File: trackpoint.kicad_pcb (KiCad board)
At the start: 2 copper layers, 27.5 x 35 mm, 32 parts, among them P1 CONN_10, P2 CONN_5, P3 CONN_8, U1 MKL03Z32VFK4, U4 ESD

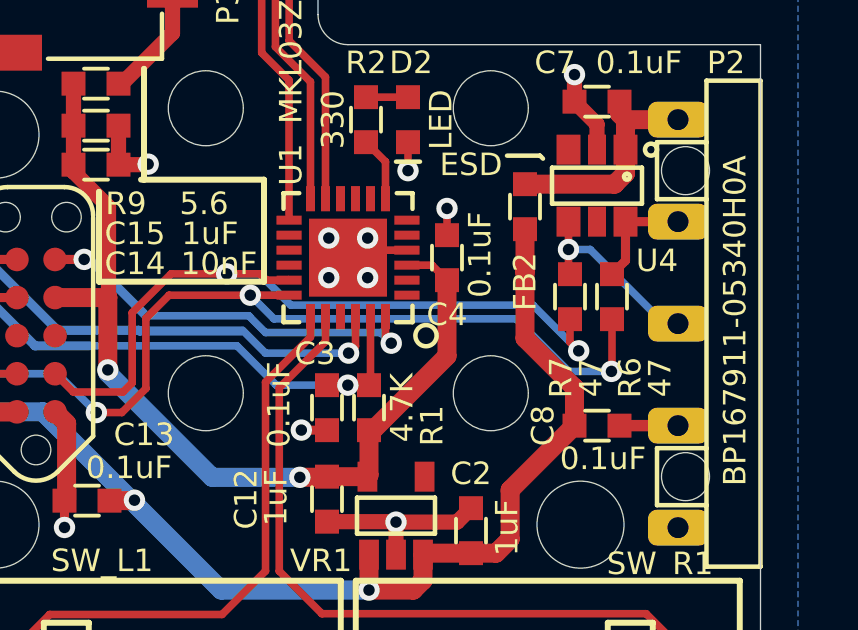
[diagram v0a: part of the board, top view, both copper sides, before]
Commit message: Adjust silk screen a tiny bit.
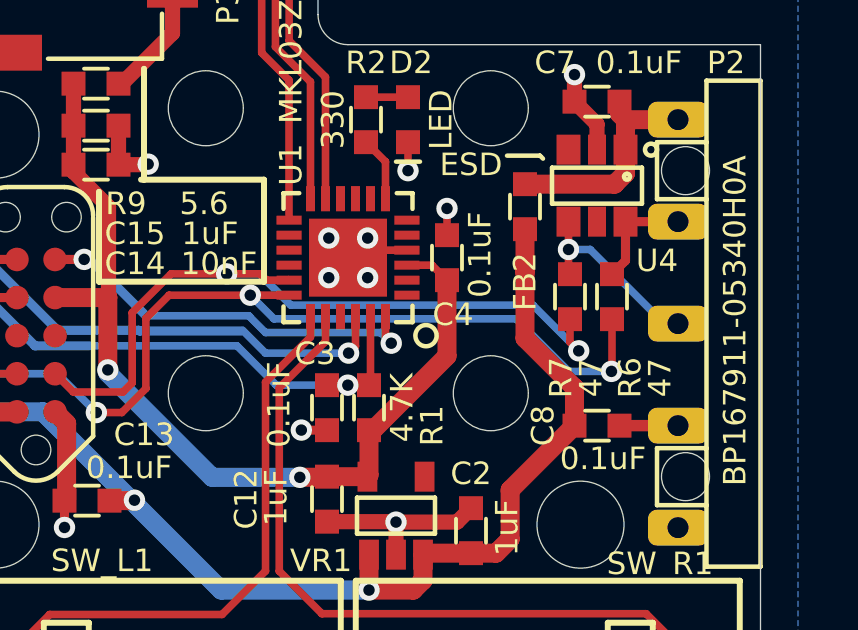
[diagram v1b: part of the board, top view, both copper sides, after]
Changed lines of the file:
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@@
     (at 209.3 130.6 270)
     (attr smd)
-    (fp_text reference C4 (at 1.9 0 180) (layer F.SilkS)
+    (fp_text reference C4 (at 1.9 -0.2 180) (layer F.SilkS)
       (effects (font (size 0.75 0.75) (thickness 0.15)))
     )

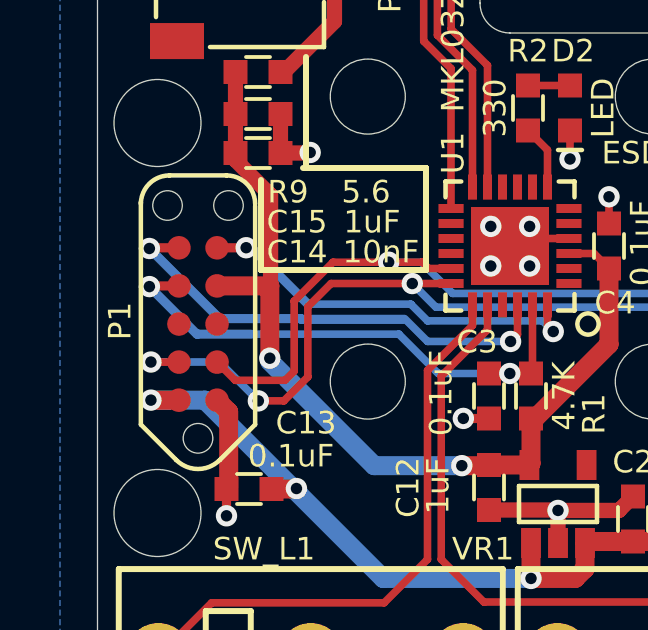
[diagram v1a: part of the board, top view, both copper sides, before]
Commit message: Add UPA14 text.
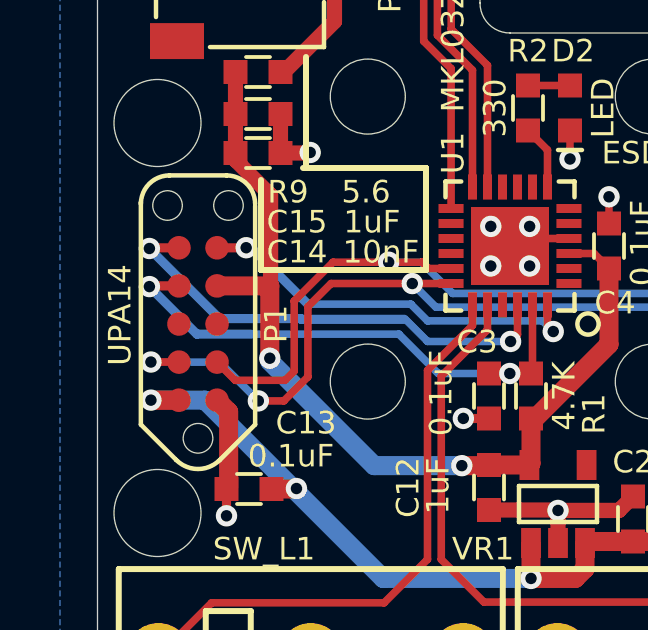
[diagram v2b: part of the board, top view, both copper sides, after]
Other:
- board text added: "UPA14"
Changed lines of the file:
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@@
   (general
     (thickness 1.6)
-    (drawings 28)
+    (drawings 29)
     (tracks 221)
     (zones 0)
@@
     (tags "Tag-Connect TC2050")
     (attr virtual)
-    (fp_text reference P1 (at 0.1 -2.6 90) (layer F.SilkS)
+    (fp_text reference P1 (at 0 2.6 90) (layer F.SilkS)
       (effects (font (size 0.75 0.75) (thickness 0.15)))
     )
@@
       (clearance 0.00001))
   )
+  (gr_text UPA14 (at 193 132.9 90) (layer F.SilkS)
+    (effects (font (size 0.75 0.75) (thickness 0.15)))
+  )
   (gr_text BP167911-05340H0A (at 218.9 132.7 90) (layer F.SilkS)

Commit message: Rename UPA14 to UPA10.
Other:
- board text added: "UPA10"
- board text removed: "UPA14"
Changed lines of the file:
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@@
-(kicad_pcb (version 20171130) (host pcbnew 5.1.3-ffb9f22~84~ubuntu18.04.1)
+(kicad_pcb (version 20171130) (host pcbnew 5.1.4-e60b266~84~ubuntu18.04.1)
   (general
     (thickness 1.6)
@@
       (clearance 0.00001))
   )
-  (gr_text UPA14 (at 193 132.9 90) (layer F.SilkS)
+  (gr_text UPA10 (at 193 132.9 90) (layer F.SilkS)
     (effects (font (size 0.75 0.75) (thickness 0.15)))
   )

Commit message: Update hole footprints and apply correct clearances.
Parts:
- removed the ? at (194.2, 126.5)
- removed the ? at (213.8, 139.5)
- removed the ? at (194.2, 139.5)
- removed the ? at (210.8, 135.1)
- removed the ? at (201.3, 135.1)
- removed the ? at (201.3, 125.6)
- removed the ? at (210.8, 125.6)
- added ?: , ugl:hole_2.9mm, F.Cu at (194.2, 126.5)
- added ?: , ugl:hole_2.9mm, F.Cu at (213.8, 139.5)
- added ?: , ugl:hole_2.9mm, F.Cu at (194.2, 139.5)
- added ?: , ugl:hole_2.5mm, F.Cu at (210.8, 135.1)
- added ?: , ugl:hole_2.5mm, F.Cu at (210.8, 125.6)
- added ?: , ugl:hole_2.5mm, F.Cu at (201.3, 135.1)
- added ?: , ugl:hole_2.5mm, F.Cu at (201.3, 125.6)

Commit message: Update microswitches.
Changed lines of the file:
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@@
     (add_net "Net-(VR1-Pad4)")
+  )
+  (module ugl:CMI126603D08 locked (layer F.Cu)
+    (at 212.660004 144.268997 180)
+    (fp_text reference SW_R1 (at -3.739996 3.468997) (layer F.SilkS)
+      (effects (font (size 0.75 0.75) (thickness 0.15)))
+    )
+    (fp_text value CMI126603D08 (at 2.060004 -2.231003) (layer F.SilkS)
+      (effects (font (size 0.75 0.75) (thickness 0.15)))
+    )
+    (fp_line (start -3.5 1.5) (end -3.5 -1.5) (layer F.SilkS) (width 0.2))
+    (fp_line (start -2 1.5) (end -3.5 1.5) (layer F.SilkS) (width 0.2))
+    (fp_line (start -2 -1.5) (end -2 1.5) (layer F.SilkS) (width 0.2))
+    (fp_line (start -3.5 -1.5) (end -2 -1.5) (layer F.SilkS) (width 0.2))
+    (fp_line (start 6.4 -2.9) (end 6.4 2.9) (layer F.SilkS) (width 0.2))
+    (fp_line (start -6.4 2.9) (end 6.4 2.9) (layer F.SilkS) (width 0.2))
+    (fp_line (start -6.4 -2.9) (end -6.4 2.9) (layer F.SilkS) (width 0.2))
+    (fp_line (start 6.4 -2.9) (end -6.4 -2.9) (layer F.SilkS) (width 0.2))
+    (pad "" np_thru_hole circle (at 5.08 0 180) (size 1.2 1.2) (drill 1.2) (layers *.Cu *.Mask))
+    (pad 2 thru_hole circle (at 0 0 180) (size 2.2 2.2) (drill 1.2) (layers *.Cu *.Mask)
+      (net 4 GND))
+    (pad 1 thru_hole circle (at -5.08 0 180) (size 2.2 2.2) (drill 1.2) (layers *.Cu *.Mask)
+      (net 27 /KEY_MRIGHT))
+  )
+  (module ugl:CMI126603D08 locked (layer F.Cu)
+    (at 199.360001 144.268997)
+    (fp_text reference SW_L1 (at -1.560001 -3.568997) (layer F.SilkS)
+      (effects (font (size 0.75 0.75) (thickness 0.15)))
+    )
+    (fp_text value CMI126603D08 (at 2.039999 2.231003) (layer F.SilkS)
+      (effects (font (size 0.75 0.75) (thickness 0.15)))
+    )
+    (fp_line (start -3.5 1.5) (end -3.5 -1.5) (layer F.SilkS) (width 0.2))
+    (fp_line (start -2 1.5) (end -3.5 1.5) (layer F.SilkS) (width 0.2))
+    (fp_line (start -2 -1.5) (end -2 1.5) (layer F.SilkS) (width 0.2))
+    (fp_line (start -3.5 -1.5) (end -2 -1.5) (layer F.SilkS) (width 0.2))
+    (fp_line (start 6.4 -2.9) (end 6.4 2.9) (layer F.SilkS) (width 0.2))
+    (fp_line (start -6.4 2.9) (end 6.4 2.9) (layer F.SilkS) (width 0.2))
+    (fp_line (start -6.4 -2.9) (end -6.4 2.9) (layer F.SilkS) (width 0.2))
+    (fp_line (start 6.4 -2.9) (end -6.4 -2.9) (layer F.SilkS) (width 0.2))
+    (pad "" np_thru_hole circle (at 5.08 0) (size 1.2 1.2) (drill 1.2) (layers *.Cu *.Mask))
+    (pad 2 thru_hole circle (at 0 0) (size 2.2 2.2) (drill 1.2) (layers *.Cu *.Mask)
+      (net 4 GND))
+    (pad 1 thru_hole circle (at -5.08 0) (size 2.2 2.2) (drill 1.2) (layers *.Cu *.Mask)
+      (net 29 /KEY_MLEFT))
   )
   (module ugl:hole_2.9mm locked (layer F.Cu)
@@
       (xy 2.621935 -1.146433)) (layer B.Mask) (width 0.01))
   )
-  (module ugl:CMI126603D08 locked (layer F.Cu)
-    (at 199.360001 144.268997)
-    (fp_text reference SW_L1 (at -1.560001 -3.568997) (layer F.SilkS)
-      (effects (font (size 0.75 0.75) (thickness 0.15)))
-    )
-    (fp_text value CMI126603D08 (at 2.039999 2.231003) (layer F.SilkS)
-      (effects (font (size 0.75 0.75) (thickness 0.15)))
-    )
-    (fp_line (start -3.5 1.5) (end -3.5 -1.5) (layer F.SilkS) (width 0.2))
-    (fp_line (start -2 1.5) (end -3.5 1.5) (layer F.SilkS) (width 0.2))
-    (fp_line (start -2 -1.5) (end -2 1.5) (layer F.SilkS) (width 0.2))
-    (fp_line (start -3.5 -1.5) (end -2 -1.5) (layer F.SilkS) (width 0.2))
-    (fp_line (start 6.4 -2.9) (end 6.4 2.9) (layer F.SilkS) (width 0.2))
-    (fp_line (start -6.4 2.9) (end 6.4 2.9) (layer F.SilkS) (width 0.2))
-    (fp_line (start -6.4 -2.9) (end -6.4 2.9) (layer F.SilkS) (width 0.2))
-    (fp_line (start 6.4 -2.9) (end -6.4 -2.9) (layer F.SilkS) (width 0.2))
-    (pad 3 thru_hole circle (at 5.08 0) (size 2.2 2.2) (drill 1.2) (layers *.Cu *.Mask))
-    (pad 2 thru_hole circle (at 0 0) (size 2.2 2.2) (drill 1.2) (layers *.Cu *.Mask)
-      (net 4 GND))
-    (pad 1 thru_hole circle (at -5.08 0) (size 2.2 2.2) (drill 1.2) (layers *.Cu *.Mask)
-      (net 29 /KEY_MLEFT))
-  )
-  (module ugl:CMI126603D08 locked (layer F.Cu)
-    (at 212.660004 144.268997 180)
-    (fp_text reference SW_R1 (at -3.739996 3.468997) (layer F.SilkS)
-      (effects (font (size 0.75 0.75) (thickness 0.15)))
-    )
-    (fp_text value CMI126603D08 (at 2.060004 -2.231003) (layer F.SilkS)
-      (effects (font (size 0.75 0.75) (thickness 0.15)))
-    )
-    (fp_line (start -3.5 1.5) (end -3.5 -1.5) (layer F.SilkS) (width 0.2))
-    (fp_line (start -2 1.5) (end -3.5 1.5) (layer F.SilkS) (width 0.2))
-    (fp_line (start -2 -1.5) (end -2 1.5) (layer F.SilkS) (width 0.2))
-    (fp_line (start -3.5 -1.5) (end -2 -1.5) (layer F.SilkS) (width 0.2))
-    (fp_line (start 6.4 -2.9) (end 6.4 2.9) (layer F.SilkS) (width 0.2))
-    (fp_line (start -6.4 2.9) (end 6.4 2.9) (layer F.SilkS) (width 0.2))
-    (fp_line (start -6.4 -2.9) (end -6.4 2.9) (layer F.SilkS) (width 0.2))
-    (fp_line (start 6.4 -2.9) (end -6.4 -2.9) (layer F.SilkS) (width 0.2))
-    (pad 3 thru_hole circle (at 5.08 0 180) (size 2.2 2.2) (drill 1.2) (layers *.Cu *.Mask))
-    (pad 2 thru_hole circle (at 0 0 180) (size 2.2 2.2) (drill 1.2) (layers *.Cu *.Mask)
-      (net 4 GND))
-    (pad 1 thru_hole circle (at -5.08 0 180) (size 2.2 2.2) (drill 1.2) (layers *.Cu *.Mask)
-      (net 27 /KEY_MRIGHT))
-  )
   (module ugl:QFN-24-1EP_4x4mm_Pitch0.5mm (layer F.Cu)

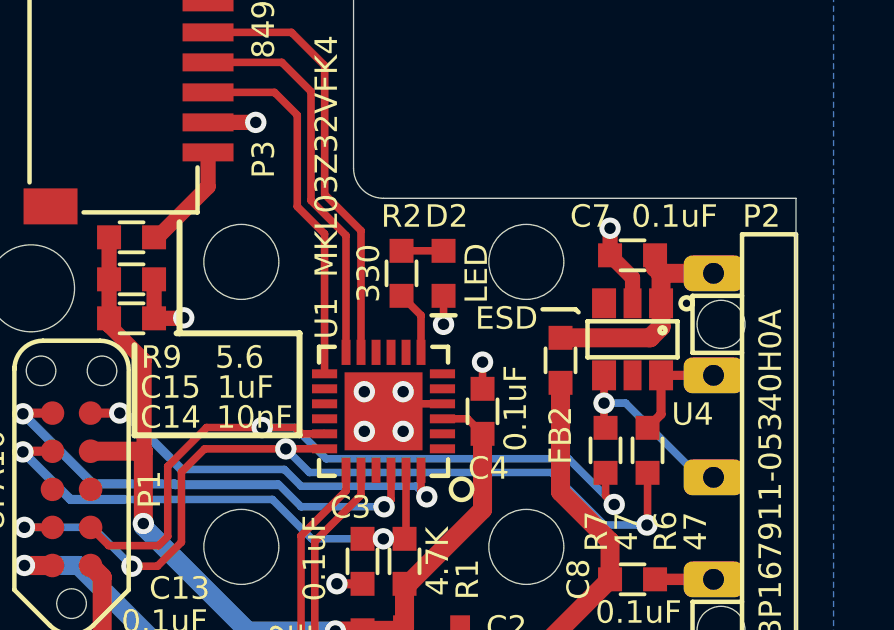
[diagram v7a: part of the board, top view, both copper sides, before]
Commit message: Update LED footprint.
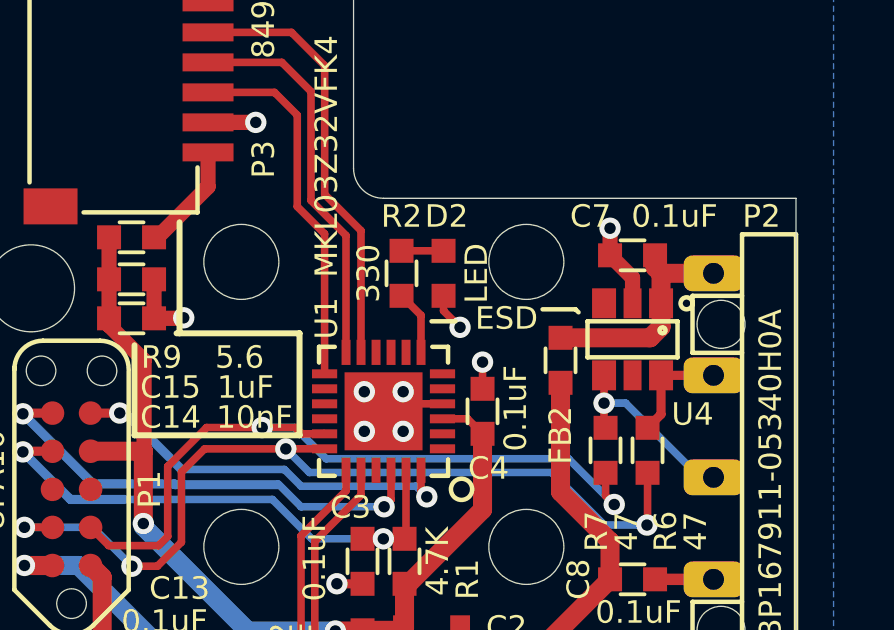
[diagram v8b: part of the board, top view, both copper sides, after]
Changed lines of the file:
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@@
     (thickness 1.6)
     (drawings 29)
-    (tracks 221)
+    (tracks 222)
     (zones 0)
     (modules 32)
@@
     (add_net "Net-(U1-Pad9)")
     (add_net "Net-(VR1-Pad4)")
+  )
+  (module ugl:SM0603_Diode (layer F.Cu)
+    (at 208 126 90)
+    (attr smd)
+    (fp_text reference D2 (at 1.9 0.1 180) (layer F.SilkS)
+      (effects (font (size 0.75 0.75) (thickness 0.15)))
+    )
+    (fp_text value LED (at 0 1.1 270) (layer F.SilkS)
+      (effects (font (size 0.75 0.75) (thickness 0.15)))
+    )
+    (fp_line (start -1.6 -0.4) (end -1.6 0.4) (layer F.SilkS) (width 0.15))
+    (pad 1 smd rect (at -0.75 0 90) (size 0.8 0.8) (layers F.Cu F.Paste F.Mask)
+      (net 4 GND))
+    (pad 2 smd rect (at 0.75 0 90) (size 0.8 0.8) (layers F.Cu F.Paste F.Mask)
+      (net 15 /TEST_LED_R))
+    (model smd\resistors\R0603.wrl
+      (offset (xyz 0 0 0.02540000082496551))
+      (scale (xyz 0.5 0.5 0.5))
+      (rotate (xyz 0 0 0))
+    )
   )
   (module ugl:CMI126603D08 locked (layer F.Cu)
@@
     )
   )
-  (module ugl:SM0603_Diode (layer F.Cu)
-    (at 208 126 90)
-    (attr smd)
-    (fp_text reference D2 (at 1.9 0.1 180) (layer F.SilkS)
-      (effects (font (size 0.75 0.75) (thickness 0.15)))
-    )
-    (fp_text value LED (at 0 1.1 270) (layer F.SilkS)
-      (effects (font (size 0.75 0.75) (thickness 0.15)))
-    )
-    (fp_line (start -1.4 -0.4) (end -1.4 0.4) (layer F.SilkS) (width 0.15))
-    (pad 1 smd rect (at -0.75 0 90) (size 0.8 0.8) (layers F.Cu F.Paste F.Mask)
-      (net 4 GND))
-    (pad 2 smd rect (at 0.75 0 90) (size 0.8 0.8) (layers F.Cu F.Paste F.Mask)
-      (net 15 /TEST_LED_R))
-    (model smd\resistors\R0603.wrl
-      (offset (xyz 0 0 0.02540000082496551))
-      (scale (xyz 0.5 0.5 0.5))
-      (rotate (xyz 0 0 0))
-    )
-  )
   (module ugl:SOT-23-5 (layer F.Cu)
     (at 207.6 139.2 180)
@@
   (segment (start 199.3218 127.5) (end 199.3392 127.4826) (width 0.508) (layer F.Cu) (net 4))
   (segment (start 198.35 127.5) (end 199.3218 127.5) (width 0.508) (layer F.Cu) (net 4))
-  (segment (start 208 126.75) (end 208 127.7) (width 0.254) (layer F.Cu) (net 4))
-  (via (at 208 127.7) (size 0.7112) (drill 0.381) (layers F.Cu B.Cu) (net 4))
+  (via (at 208.55 127.8) (size 0.7112) (drill 0.381) (layers F.Cu B.Cu) (net 4))
   (segment (start 196.55 138.7) (end 196.55 139.5936) (width 0.3048) (layer F.Cu) (net 4))
   (via (at 196.55 139.5936) (size 0.7112) (drill 0.381) (layers F.Cu B.Cu) (net 4))
   (segment (start 196.6214 136.1264) (end 196.6214 138.6586) (width 0.635) (layer F.Cu) (net 4))
   (segment (start 196.235 135.74) (end 196.6214 136.1264) (width 0.635) (layer F.Cu) (net 4))
+  (segment (start 208 126.75) (end 208 127.25) (width 0.254) (layer F.Cu) (net 4))
+  (segment (start 208 127.25) (end 208.55 127.8) (width 0.254) (layer F.Cu) (net 4))
   (segment (start 206.75 134.8) (end 206.7 134.85) (width 0.254) (layer F.Cu) (net 5))
   (segment (start 206.75 132.565) (end 206.75 134.8) (width 0.254) (layer F.Cu) (net 5))
